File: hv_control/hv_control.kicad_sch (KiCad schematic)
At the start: 176 parts, among them J1 DB9, J10 x, J11 Conn_02x03_Odd_Even, J12 x, J13 Conn_01x02_Male, J14 Conn_01x02_Male, J15 Conn_01x01_Pin, J16 Conn_01x02_Male, J17 Conn_01x02_Male, J18 Conn_01x01_Pin, J19 Conn_01x01_Pin, J2 DB15, J3 INPUTS, J4 I/O, J5 USB_B_Mini, J6 Conn_01x01_Pin, J7 Conn_01x01_Male, J8 Conn_02x04_Odd_Even, J9 x, K1 RELAY_DPDT, K2 RELAY_DPDT, M1 Fan_4pin, P2 SWD, Q1 BSS138, Q2 BSS138, Q3 BSS138, Q4 BSS138, U1 XMC4400-F100, U10 XMC1301T016F0032ABXUMA1, U11 LT1764EQ, U12 TLV9064, U13 DRV8870DDA, U14 AD8226, U15 MAX3463, U18 LT1764EQ, U19 KSZ8081, U2 ips511g, U20 ETH100_MAG, U21 MAX3463, U22 MAX3463, U23 MAX3463, U3 ips511g, U4 MAX3463, U5 AD8226, U6 R-78E5.0-0.5, U7 ${SIM.PARAMS}, U8 R-78E3.3-0.5, U9 ISO7321C, Y1 12MHz, Y2 25MHz

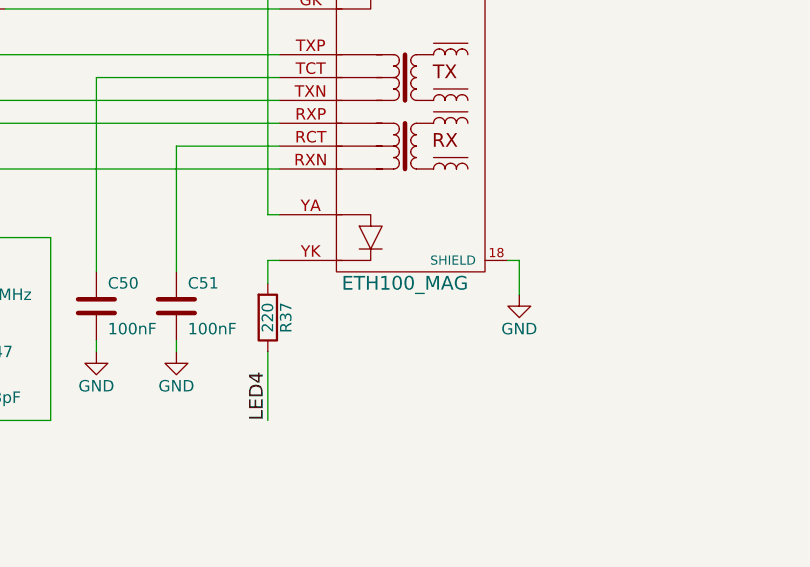
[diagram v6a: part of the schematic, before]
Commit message: Adding initial hal files for linuxcnc
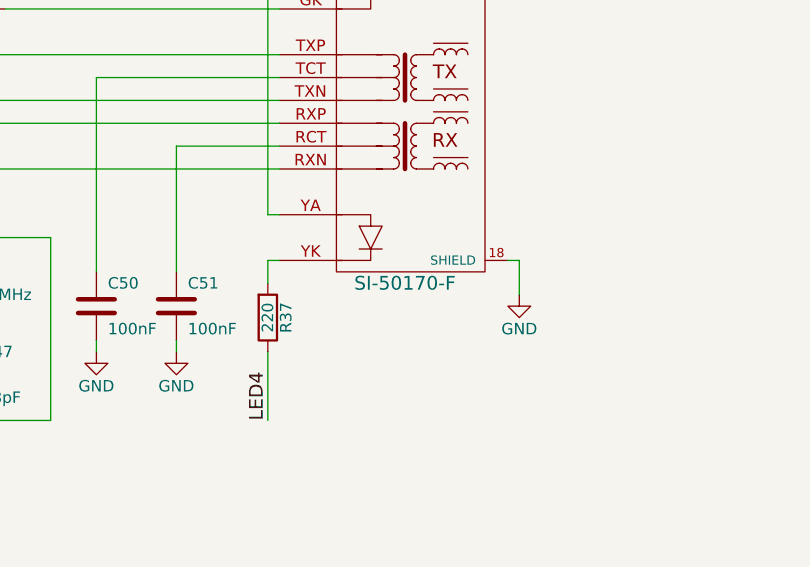
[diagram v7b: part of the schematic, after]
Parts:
- U20: value ETH100_MAG -> SI-50170-F
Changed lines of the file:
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@@
       (effects (font (size 1.524 1.524)))
     )
-    (property "Value" "ETH100_MAG" (at 256.54 129.54 0)
+    (property "Value" "SI-50170-F" (at 256.54 129.54 0)
       (effects (font (size 1.524 1.524)))
     )

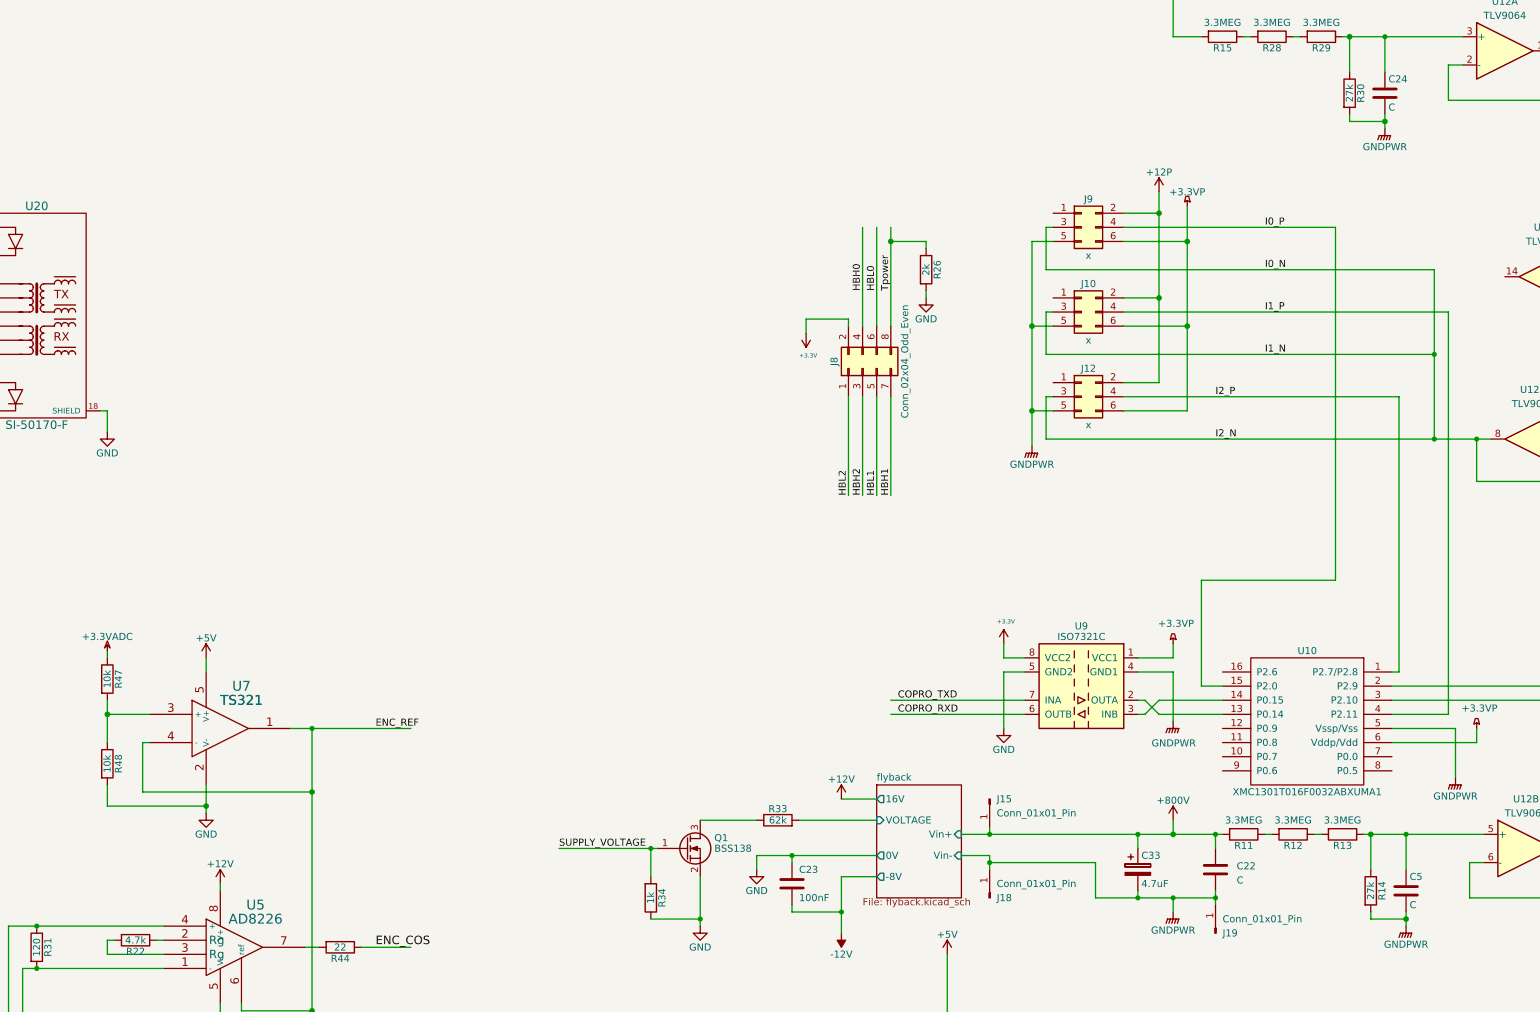
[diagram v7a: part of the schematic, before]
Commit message: Adding cpuinfo.m
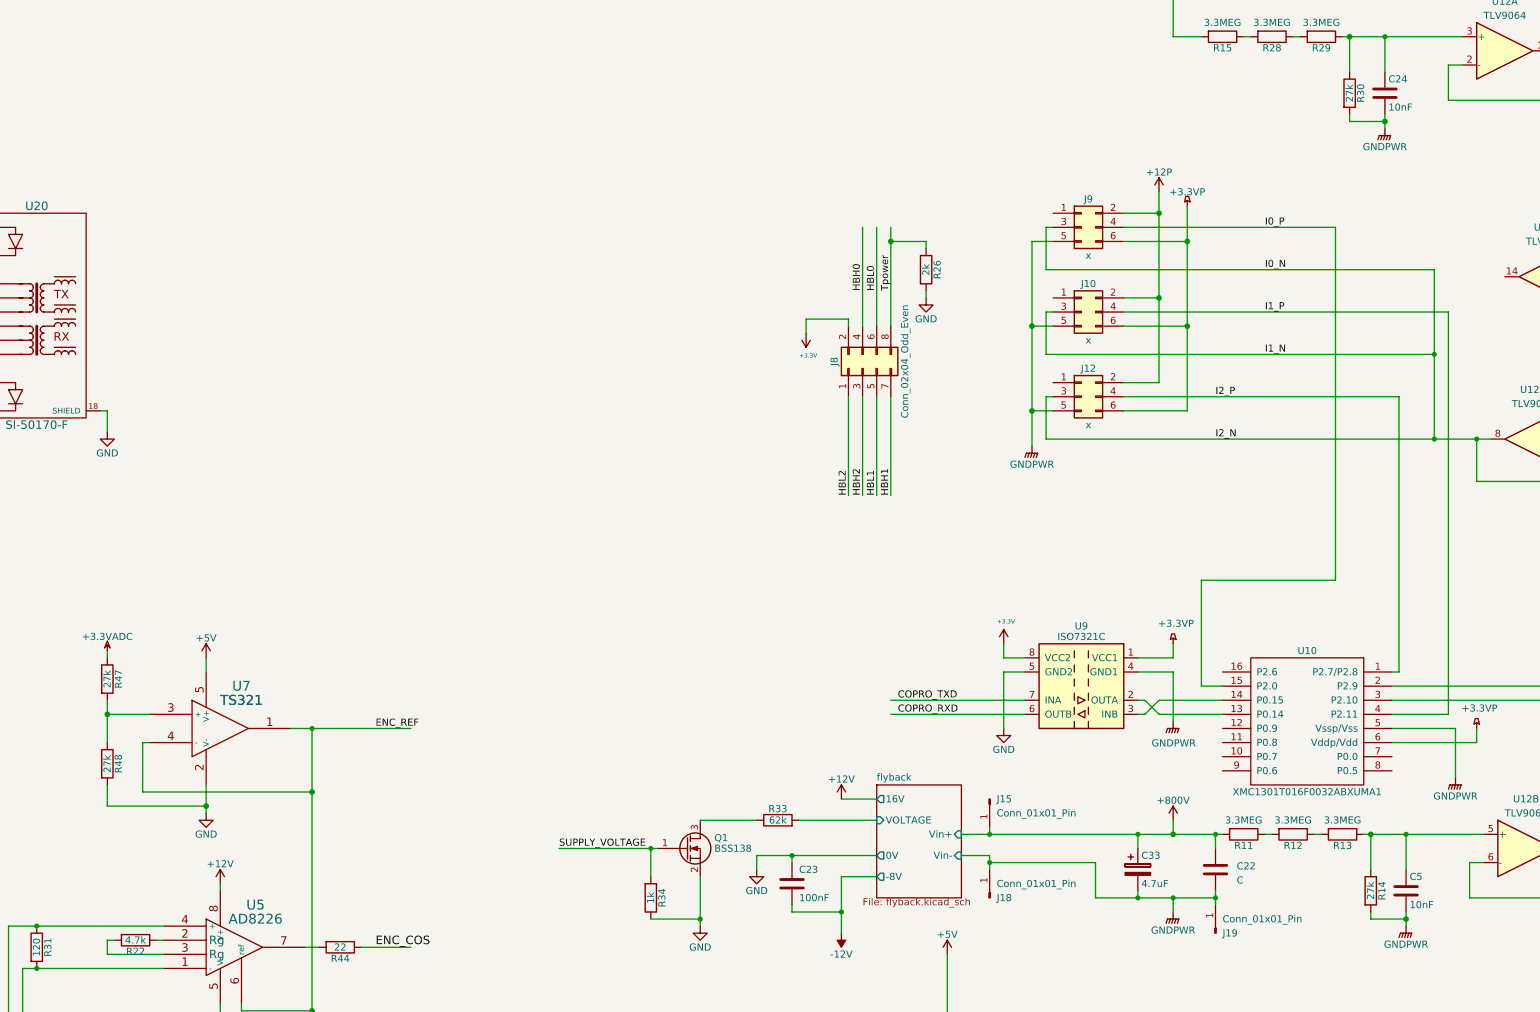
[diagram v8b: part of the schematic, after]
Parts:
- C24, C5: value C -> 10nF
- R47, R48: value 10k -> 27k
- U1: Mouser (none) -> 726-MC4400F100F512BA
- U10: Mouser (none) -> 726-1301T016F0032ABX
- U14, U5: Mouser (none) -> 584-AD8226ARZ-R7
- U19: Mouser (none) -> 998-KSZ8081RNACA
- U20: Mouser (none) -> 530-SI-50170-F
- U7: Mouser (none) -> 511-TS321AIL
- U9: Mouser (none) -> 595-ISO7321CDR
- Y1: Mouser (none) -> 520-120-12-33-AENT
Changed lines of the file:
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@@
       (effects (font (size 1.27 1.27)) hide)
     )
+    (property "Mouser" "520-120-12-33-AENT" (at 113.03 255.27 0)
+      (effects (font (size 1.27 1.27)) hide)
+    )
     (pin "1")
     (pin "2")
@@
       (effects (font (size 1.27 1.27)) hide)
     )
+    (property "Mouser" "584-AD8226ARZ-R7" (at 292.1 223.52 0)
+      (effects (font (size 1.27 1.27)) hide)
+    )
     (pin "1")
     (pin "2")
@@
       (effects (font (size 1.524 1.524)) hide)
     )
+    (property "Mouser" "998-KSZ8081RNACA" (at 176.53 113.03 0)
+      (effects (font (size 1.27 1.27)) hide)
+    )
     (pin "1")
     (pin "10")
@@
       (effects (font (size 1.27 1.27)) hide)
     )
+    (property "Mouser" "584-AD8226ARZ-R7" (at 292.1 259.08 0)
+      (effects (font (size 1.27 1.27)) hide)
+    )
     (pin "1")
     (pin "2")
@@
       (effects (font (size 1.524 1.524)) hide)
     )
+    (property "Mouser" " 530-SI-50170-F" (at 256.54 110.49 0)
+      (effects (font (size 1.27 1.27)) hide)
+    )
     (pin "18")
     (pin "GA")
@@
       (effects (font (size 1.27 1.27)))
     )
-    (property "Value" "10k" (at 269.24 190.5 90)
+    (property "Value" "27k" (at 269.24 190.5 90)
       (effects (font (size 1.27 1.27)))
     )
@@
       (effects (font (size 1.27 1.27)))
     )
-    (property "Value" "10k" (at 269.24 175.26 90)
+    (property "Value" "27k" (at 269.24 175.26 90)
       (effects (font (size 1.27 1.27)))
     )
@@
       (effects (font (size 1.524 1.524)) hide)
     )
+    (property "Mouser" "726-MC4400F100F512BA" (at 27.94 93.98 0)
+      (effects (font (size 1.27 1.27)) hide)
+    )
     (pin "1")
     (pin "10")
@@
       (effects (font (size 1.524 1.524)) hide)
     )
+    (property "Mouser" "726-MC4400F100F512BA" (at 27.94 179.07 0)
+      (effects (font (size 1.27 1.27)) hide)
+    )
     (pin "1")
     (pin "10")
@@
       (effects (font (size 1.524 1.524)) hide)
     )
+    (property "Mouser" "726-MC4400F100F512BA" (at 27.94 252.73 0)
+      (effects (font (size 1.27 1.27)) hide)
+    )
     (pin "1")
     (pin "10")
@@
       (effects (font (size 1.524 1.524)) hide)
     )
+    (property "Mouser" "726-MC4400F100F512BA" (at 27.94 326.39 0)
+      (effects (font (size 1.27 1.27)) hide)
+    )
     (pin "1")
     (pin "10")
@@
       (effects (font (size 1.27 1.27)) hide)
     )
+    (property "Mouser" "726-1301T016F0032ABX " (at 485.14 182.88 0)
+      (effects (font (size 1.27 1.27)) hide)
+    )
     (pin "1")
     (pin "10")
@@
       (effects (font (size 1.524 1.524)) hide)
     )
+    (property "Mouser" "511-TS321AIL" (at 289.56 184.15 0)
+      (effects (font (size 1.27 1.27)) hide)
+    )
     (pin "1")
     (pin "2")
@@
       (effects (font (size 1.27 1.27)) hide)
     )
+    (property "Mouser" "595-ISO7321CDR" (at 444.5 176.53 0)
+      (effects (font (size 1.27 1.27)) hide)
+    )
     (pin "1")
     (pin "2")
@@
       (effects (font (size 1.27 1.27)) (justify left))
     )
-    (property "Value" "C" (at 503.555 215.9 0)
+    (property "Value" "10nF" (at 503.555 215.9 0)
       (effects (font (size 1.27 1.27)) (justify left))
     )
@@
       (effects (font (size 1.27 1.27)) (justify left))
     )
-    (property "Value" "C" (at 499.745 72.39 0)
+    (property "Value" "10nF" (at 499.745 72.39 0)
       (effects (font (size 1.27 1.27)) (justify left))
     )
